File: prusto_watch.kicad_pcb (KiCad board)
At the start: 2 copper layers, 54 parts, among them J1 USB_microB_2040002-1, J2 Conn_02x05_Odd_Even, J3 Vibration Motor, J4 Conn_01x06, J5 Conn_01x08, J6 Conn_02x03_Odd_Even, Q3 RUM002N02T2L, SW2 SW_Push, U1 STM32F303RCT6-48, U2 LTC4063, U3 LIS3DETR, U5 TPS60241DGKR, U7 RT9818A-18GV, U8 WM1389CT-ND, Y1 ECS.327, Y2 FA-238

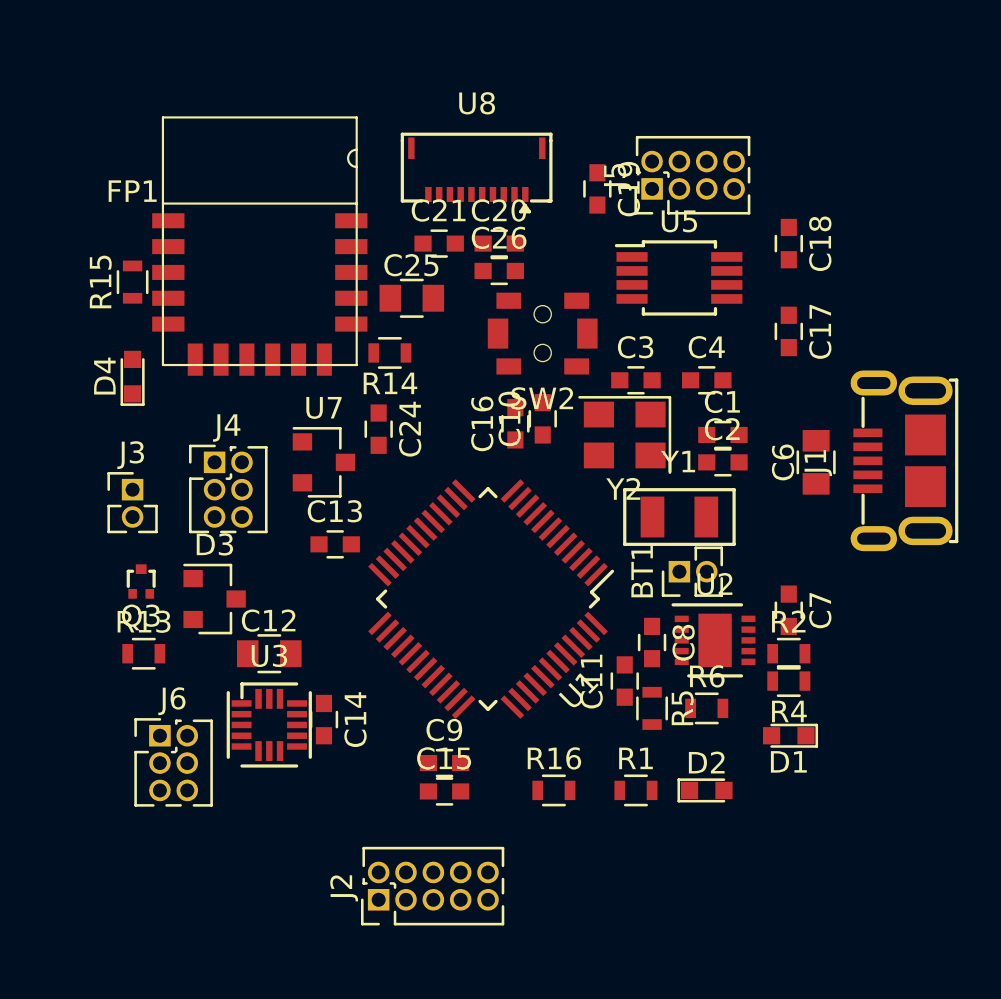
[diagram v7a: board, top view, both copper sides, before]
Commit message: First pass at PCB placement
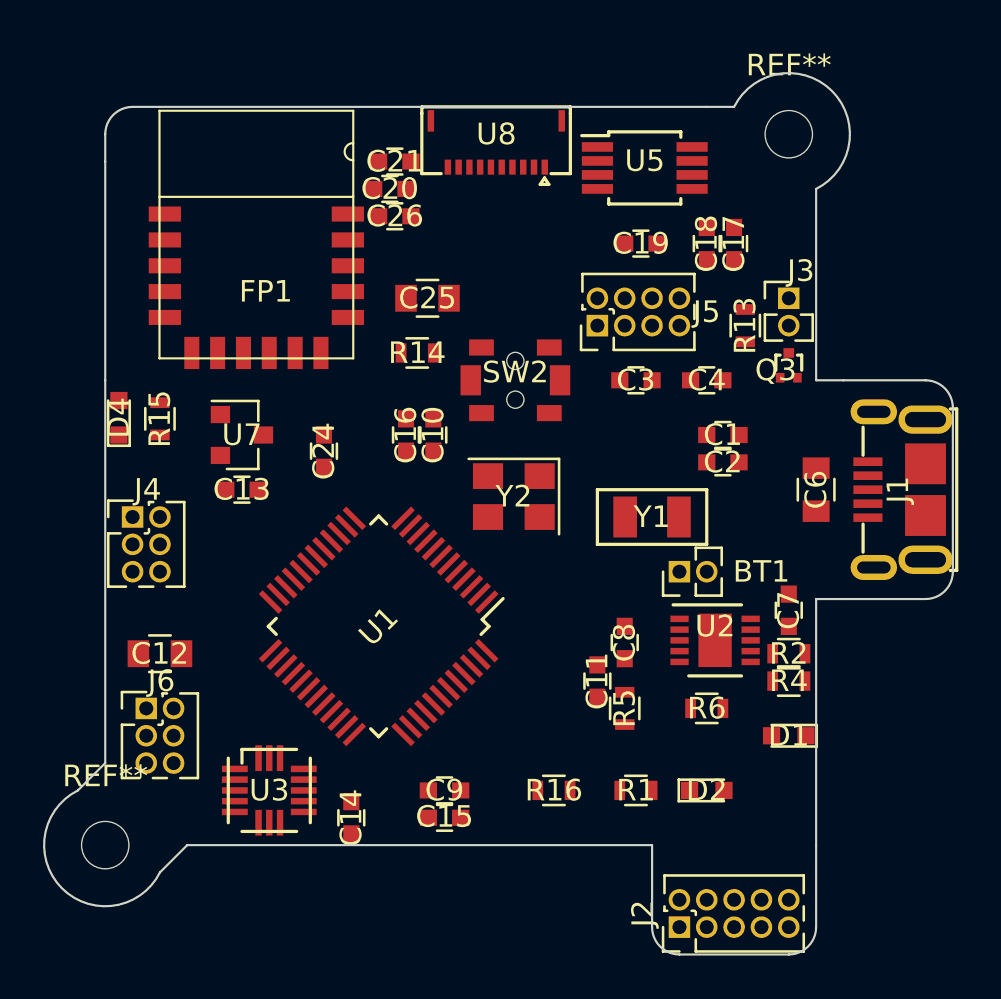
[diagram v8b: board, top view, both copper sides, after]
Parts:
- removed D3: BAT54, TO_SOT_Packages_SMD:SOT-23
- added REF**: MountingHole_2.2mm_M2, Mounting_Holes:MountingHole_2.2mm_M2, F.Cu at (161.3, 82.5)
- added REF**: MountingHole_2.2mm_M2, Mounting_Holes:MountingHole_2.2mm_M2, F.Cu at (129.5, 115.6)
- FP1: value BM71BLES1FC2 -> RN4871
- U2: footprint Housings_DFN_QFN:DFN-10-1EP_3x3mm_Pitch0.5mm -> prusto_watch:DFN-10-1EP_3x3mm_Pitch0.5mm
- moved R13 31.8 mm to (159.3, 91.4), turned to 90 degrees
- moved J3 31.7 mm to (161.3, 90.2)
- moved Q3 31.7 mm to (161.3, 92.7)
- moved J2 14.0 mm to (156.2, 119.4)
- moved J5 6.84 mm to (152.4, 91.4)
- moved R15 6.48 mm to (132.1, 95.8)
- moved Y2 5.89 mm to (148.5, 99.4)
- moved C20 5.68 mm to (142.8, 85.1)
- moved C26 5.47 mm to (143.0, 86.4)
- moved U5 5.36 mm to (154.6, 84.1)
- moved U1 5.24 mm to (142.2, 105.4)
- moved C10 5.14 mm to (144.8, 96.5)
- moved C16 5.11 mm to (143.5, 96.5)
- moved C12 5.08 mm to (132.1, 106.7)
- moved C13 5.02 mm to (135.9, 99.1), turned to 180 degrees
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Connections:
- U1 pad 30: (no net) -> /ACC_INT1
- U1 pad 31: (no net) -> /ACC_INT2
- U3 pad 11: (no net) -> /ACC_INT1
- U3 pad 9: (no net) -> /ACC_INT2
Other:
- board outline added: 42.2 x 40.9 mm
- net class Default: clearance 0.2 -> 0.1778; trace_width 0.25 -> 0.254
- rule trace_clearance: 0.2 -> 0.1778
- rule trace_min: 0.2 -> 0.1524
